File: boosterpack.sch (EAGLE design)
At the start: 38 parts, among them J1 POWERPOLE_DOUBLE, J2 PHOENIXSCREWTERMINAL_2, J3 PHOENIXSCREWTERMINAL_2

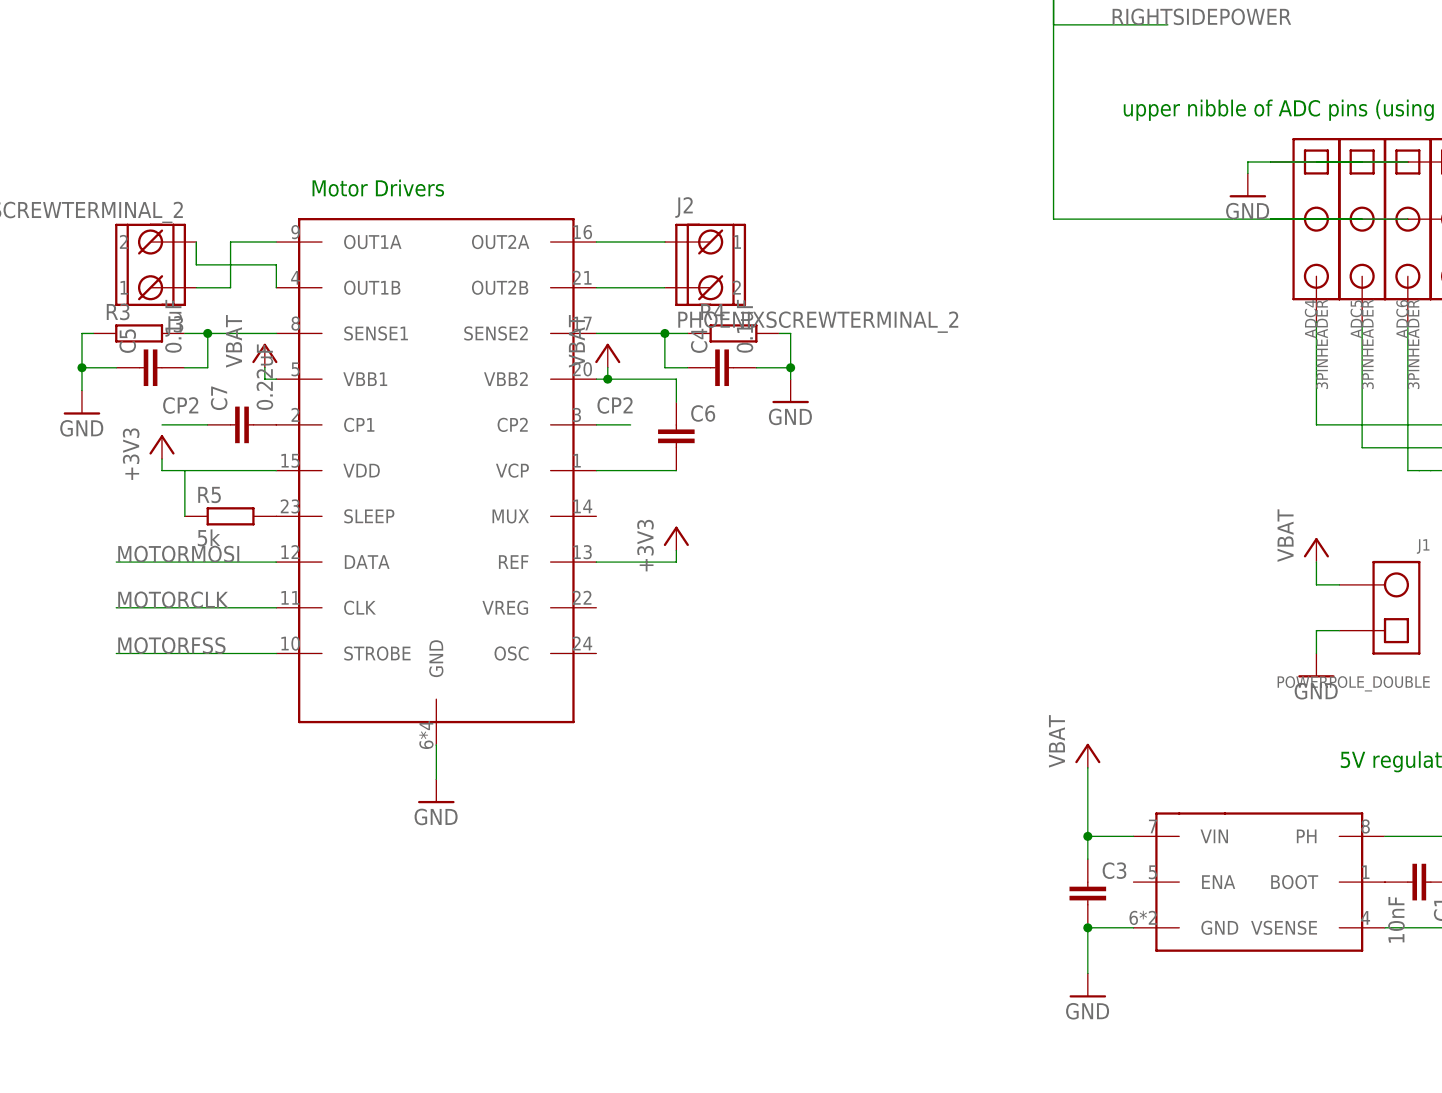
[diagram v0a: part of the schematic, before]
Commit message: shrank the board; added decopling cap for power
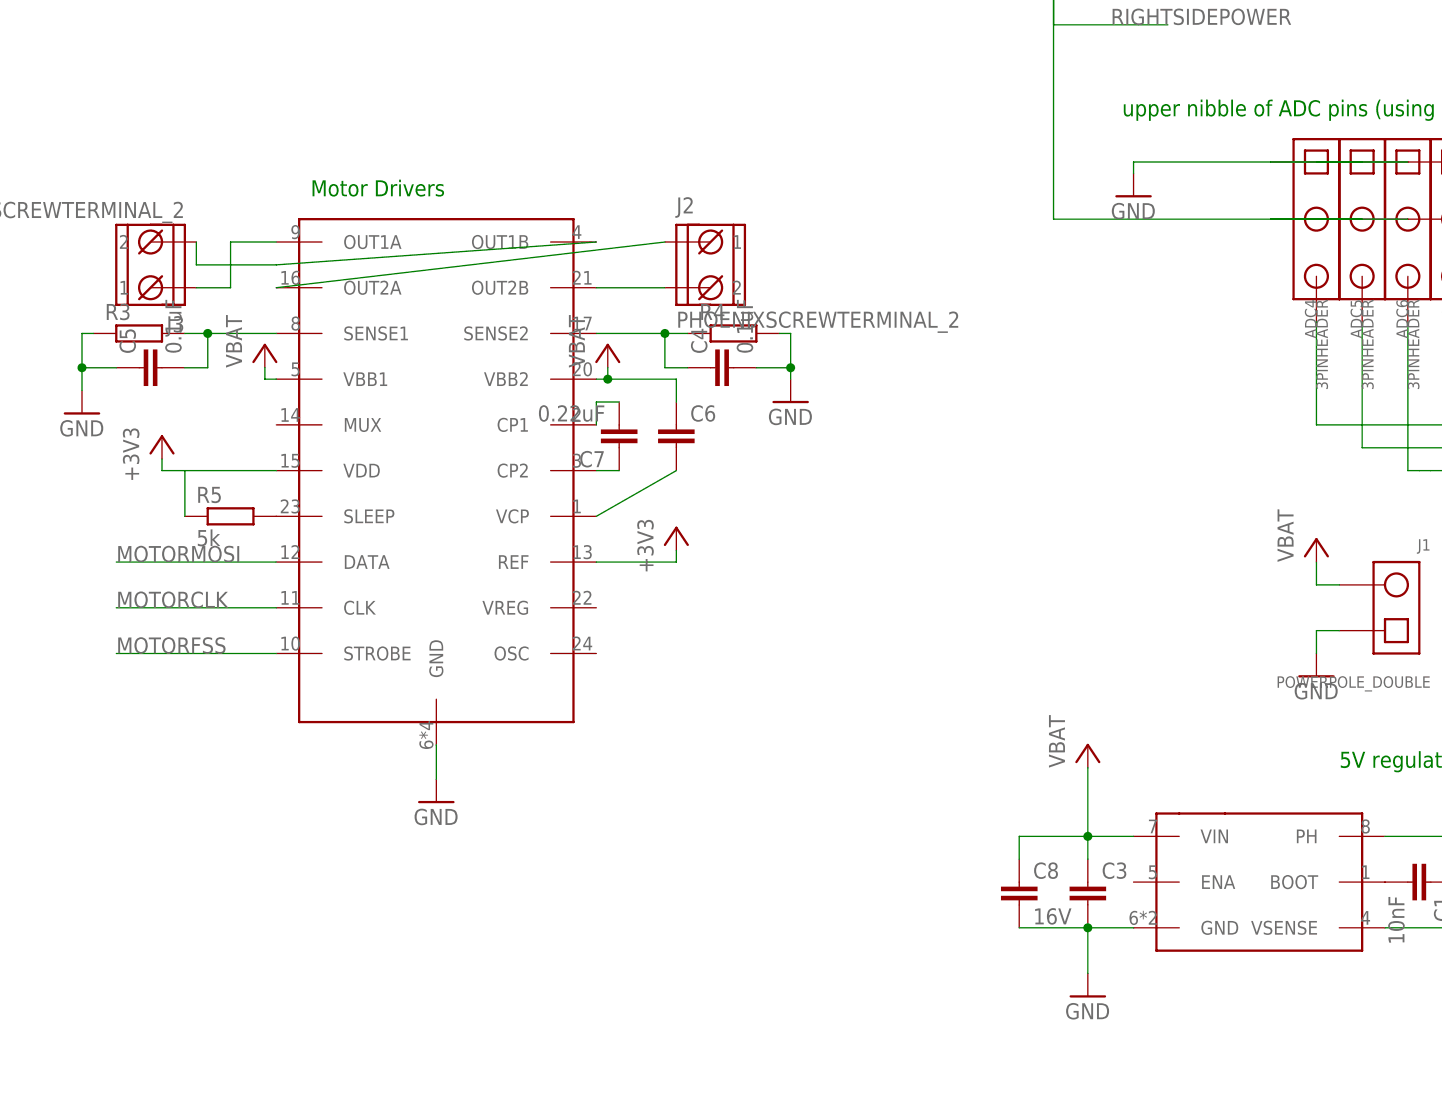
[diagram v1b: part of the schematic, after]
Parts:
- added C8: 16V, resistor:C-EU050-075X075
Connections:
- net CP2 renamed N$23
- net GND: now also C8.2
- net VCC: now also C8.1
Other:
- moved on the sheet: C7
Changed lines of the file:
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@@
 <grid distance="0.05" unitdist="inch" unit="inch" style="lines" multiple="1" display="no" altdistance="0.01" altunitdist="inch" altunit="inch"/>
 <layers>
-<layer number="1" name="Top" color="4" fill="1" visible="yes" active="no"/>
-<layer number="16" name="Bottom" color="1" fill="1" visible="yes" active="no"/>
-<layer number="17" name="Pads" color="2" fill="1" visible="yes" active="no"/>
-<layer number="18" name="Vias" color="2" fill="1" visible="yes" active="no"/>
-<layer number="19" name="Unrouted" color="6" fill="1" visible="yes" active="no"/>
-<layer number="20" name="Dimension" color="15" fill="1" visible="yes" active="no"/>
-<layer number="21" name="tPlace" color="7" fill="1" visible="yes" active="no"/>
-<layer number="22" name="bPlace" color="7" fill="1" visible="yes" active="no"/>
-<layer number="23" name="tOrigins" color="15" fill="1" visible="yes" active="no"/>
-<layer number="24" name="bOrigins" color="15" fill="1" visible="yes" active="no"/>
-<layer number="25" name="tNames" color="7" fill="1" visible="yes" active="no"/>
-<layer number="26" name="bNames" color="7" fill="1" visible="yes" active="no"/>
-<layer number="27" name="tValues" color="7" fill="1" visible="yes" active="no"/>
-<layer number="28" name="bValues" color="7" fill="1" visible="yes" active="no"/>
+<layer number="1" name="Top" color="4" fill="1" visible="no" active="no"/>
+<layer number="16" name="Bottom" color="1" fill="1" visible="no" active="no"/>
+<layer number="17" name="Pads" color="2" fill="1" visible="no" active="no"/>
+<layer number="18" name="Vias" color="2" fill="1" visible="no" active="no"/>
+<layer number="19" name="Unrouted" color="6" fill="1" visible="no" active="no"/>
+<layer number="20" name="Dimension" color="15" fill="1" visible="no" active="no"/>
+<layer number="21" name="tPlace" color="7" fill="1" visible="no" active="no"/>
+<layer number="22" name="bPlace" color="7" fill="1" visible="no" active="no"/>
+<layer number="23" name="tOrigins" color="15" fill="1" visible="no" active="no"/>
+<layer number="24" name="bOrigins" color="15" fill="1" visible="no" active="no"/>
+<layer number="25" name="tNames" color="7" fill="1" visible="no" active="no"/>
+<layer number="26" name="bNames" color="7" fill="1" visible="no" active="no"/>
+<layer number="27" name="tValues" color="7" fill="1" visible="no" active="no"/>
+<layer number="28" name="bValues" color="7" fill="1" visible="no" active="no"/>
 <layer number="29" name="tStop" color="7" fill="3" visible="no" active="no"/>
 <layer number="30" name="bStop" color="7" fill="6" visible="no" active="no"/>
@@
 <layer number="35" name="tGlue" color="7" fill="4" visible="no" active="no"/>
 <layer number="36" name="bGlue" color="7" fill="5" visible="no" active="no"/>
-<layer number="37" name="tTest" color="7" fill="1" visible="yes" active="no"/>
-<layer number="38" name="bTest" color="7" fill="1" visible="yes" active="no"/>
+<layer number="37" name="tTest" color="7" fill="1" visible="no" active="no"/>
+<layer number="38" name="bTest" color="7" fill="1" visible="no" active="no"/>
 <layer number="39" name="tKeepout" color="4" fill="11" visible="no" active="no"/>
 <layer number="40" name="bKeepout" color="1" fill="11" visible="no" active="no"/>
@@
 <layer number="44" name="Drills" color="7" fill="1" visible="no" active="no"/>
 <layer number="45" name="Holes" color="7" fill="1" visible="no" active="no"/>
-<layer number="46" name="Milling" color="3" fill="1" visible="yes" active="no"/>
-<layer number="47" name="Measures" color="7" fill="1" visible="yes" active="no"/>
-<layer number="48" name="Document" color="7" fill="1" visible="yes" active="no"/>
-<layer number="49" name="Reference" color="7" fill="1" visible="yes" active="no"/>
-<layer number="50" name="dxf" color="7" fill="1" visible="yes" active="no"/>
-<layer number="51" name="tDocu" color="7" fill="1" visible="yes" active="no"/>
-<layer number="52" name="bDocu" color="7" fill="1" visible="yes" active="no"/>
-<layer number="53" name="tGND_GNDA" color="7" fill="9" visible="yes" active="no"/>
-<layer number="54" name="bGND_GNDA" color="1" fill="9" visible="yes" active="no"/>
-<layer number="56" name="wert" color="7" fill="1" visible="yes" active="no"/>
-<layer number="59" name="tCarbon" color="7" fill="1" visible="yes" active="no"/>
-<layer number="60" name="bCarbon" color="7" fill="1" visible="yes" active="no"/>
+<layer number="46" name="Milling" color="3" fill="1" visible="no" active="no"/>
+<layer number="47" name="Measures" color="7" fill="1" visible="no" active="no"/>
+<layer number="48" name="Document" color="7" fill="1" visible="no" active="no"/>
+<layer number="49" name="Reference" color="7" fill="1" visible="no" active="no"/>
+<layer number="50" name="dxf" color="7" fill="1" visible="no" active="no"/>
+<layer number="51" name="tDocu" color="7" fill="1" visible="no" active="no"/>
+<layer number="52" name="bDocu" color="7" fill="1" visible="no" active="no"/>
+<layer number="53" name="tGND_GNDA" color="7" fill="9" visible="no" active="no"/>
+<layer number="54" name="bGND_GNDA" color="1" fill="9" visible="no" active="no"/>
+<layer number="56" name="wert" color="7" fill="1" visible="no" active="no"/>
+<layer number="59" name="tCarbon" color="7" fill="1" visible="no" active="no"/>
+<layer number="60" name="bCarbon" color="7" fill="1" visible="no" active="no"/>
 <layer number="91" name="Nets" color="2" fill="1" visible="yes" active="yes"/>
 <layer number="92" name="Busses" color="1" fill="1" visible="yes" active="yes"/>
@@
 <part name="+3V6" library="supply1" deviceset="+3V3" device=""/>
 <part name="+3V7" library="supply1" deviceset="+3V3" device=""/>
+<part name="C8" library="resistor" deviceset="C-EU" device="050-075X075" value="16V"/>
 </parts>
 <sheets>
@@
 <instance part="+3V3" gate="G$1" x="53.34" y="33.02"/>
 <instance part="GND7" gate="1" x="134.62" y="86.36"/>
-<instance part="GND8" gate="1" x="-2.54" y="73.66"/>
+<instance part="GND8" gate="1" x="-15.24" y="73.66"/>
 <instance part="D1" gate="G$1" x="25.4" y="-3.81" rot="R90"/>
 <instance part="U$3" gate="G$1" x="-92.71" y="17.78"/>
@@
 <instance part="C6" gate="G$1" x="-66.04" y="48.26"/>
 <instance part="R5" gate="G$1" x="-115.57" y="38.1"/>
-<instance part="C7" gate="G$1" x="-115.57" y="48.26" rot="R90"/>
+<instance part="C7" gate="G$1" x="-72.39" y="45.72" rot="R180"/>
 <instance part="+3V6" gate="G$1" x="-123.19" y="46.99"/>
 <instance part="+3V7" gate="G$1" x="-66.04" y="36.83"/>
+<instance part="C8" gate="G$1" x="-27.94" y="-2.54"/>
 </instances>
 <busses>
@@
 <wire x1="-20.32" y1="-7.62" x2="-15.24" y2="-7.62" width="0.1524" layer="91"/>
 <junction x="-20.32" y="-7.62"/>
+<pinref part="C8" gate="G$1" pin="2"/>
+<wire x1="-20.32" y1="-7.62" x2="-27.94" y2="-7.62" width="0.1524" layer="91"/>
 </segment>
 <segment>
@@
 <pinref part="ADC4" gate="G$1" pin="1"/>
 <pinref part="GND8" gate="1" pin="GND"/>
-<wire x1="0" y1="77.47" x2="-2.54" y2="77.47" width="0.1524" layer="91"/>
+<wire x1="0" y1="77.47" x2="-15.24" y2="77.47" width="0.1524" layer="91"/>
 <pinref part="ADC5" gate="G$1" pin="1"/>
 <pinref part="ADC6" gate="G$1" pin="1"/>
@@
 <wire x1="15.24" y1="77.47" x2="5.08" y2="77.47" width="0.1524" layer="91"/>
 <wire x1="5.08" y1="77.47" x2="0" y2="77.47" width="0.1524" layer="91"/>
-<wire x1="-2.54" y1="77.47" x2="-2.54" y2="76.2" width="0.1524" layer="91"/>
+<wire x1="-15.24" y1="77.47" x2="-15.24" y2="76.2" width="0.1524" layer="91"/>
 </segment>
 <segment>
@@
 <wire x1="-20.32" y1="10.16" x2="-20.32" y2="2.54" width="0.1524" layer="91"/>
 <junction x="-20.32" y="2.54"/>
+<pinref part="C8" gate="G$1" pin="1"/>
+<wire x1="-20.32" y1="2.54" x2="-27.94" y2="2.54" width="0.1524" layer="91"/>
+<wire x1="-27.94" y1="2.54" x2="-27.94" y2="0" width="0.1524" layer="91"/>
 </segment>
 <segment>
@@
 <pinref part="J2" gate="G$1" pin="1"/>
 <pinref part="U$3" gate="G$1" pin="OUT2A"/>
-<wire x1="-67.31" y1="68.58" x2="-74.93" y2="68.58" width="0.1524" layer="91"/>
+<wire x1="-67.31" y1="68.58" x2="-110.49" y2="63.5" width="0.1524" layer="91"/>
 </segment>
 </net>
@@
 <pinref part="U$3" gate="G$1" pin="VCP"/>
 <pinref part="C6" gate="G$1" pin="2"/>
-<wire x1="-74.93" y1="43.18" x2="-66.04" y2="43.18" width="0.1524" layer="91"/>
+<wire x1="-74.93" y1="38.1" x2="-66.04" y2="43.18" width="0.1524" layer="91"/>
 </segment>
 </net>
@@
 <pinref part="U$3" gate="G$1" pin="SLEEP"/>
 <pinref part="R5" gate="G$1" pin="2"/>
-</segment>
-</net>
-<net name="CP2" class="0">
-<segment>
-<pinref part="U$3" gate="G$1" pin="CP2"/>
-<wire x1="-74.93" y1="48.26" x2="-71.12" y2="48.26" width="0.1524" layer="91"/>
-<label x="-74.93" y="49.53" size="1.778" layer="95"/>
-</segment>
-<segment>
-<pinref part="C7" gate="G$1" pin="1"/>
-<wire x1="-118.11" y1="48.26" x2="-123.19" y2="48.26" width="0.1524" layer="91"/>
-<label x="-123.19" y="49.53" size="1.778" layer="95"/>
-</segment>
-</net>
-<net name="N$23" class="0">
-<segment>
-<pinref part="U$3" gate="G$1" pin="CP1"/>
-<pinref part="C7" gate="G$1" pin="2"/>
 </segment>
 </net>
@@
 <segment>
 <pinref part="U$3" gate="G$1" pin="OUT1B"/>
-<wire x1="-110.49" y1="63.5" x2="-110.49" y2="66.04" width="0.1524" layer="91"/>
+<wire x1="-74.93" y1="68.58" x2="-110.49" y2="66.04" width="0.1524" layer="91"/>
 <pinref part="J3" gate="G$1" pin="2"/>
 <wire x1="-110.49" y1="66.04" x2="-119.38" y2="66.04" width="0.1524" layer="91"/>
@@
 </segment>
 </net>
+<net name="N$23" class="0">
+<segment>
+<pinref part="U$3" gate="G$1" pin="CP2"/>
+<pinref part="C7" gate="G$1" pin="1"/>
+<wire x1="-74.93" y1="43.18" x2="-72.39" y2="43.18" width="0.1524" layer="91"/>
+</segment>
+</net>
+<net name="N$28" class="0">
+<segment>
+<pinref part="C7" gate="G$1" pin="2"/>
+<pinref part="U$3" gate="G$1" pin="CP1"/>
+<wire x1="-72.39" y1="50.8" x2="-74.93" y2="50.8" width="0.1524" layer="91"/>
+<wire x1="-74.93" y1="50.8" x2="-74.93" y2="48.26" width="0.1524" layer="91"/>
+</segment>
+</net>

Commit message: increased the spacing between the leads of all resistors and some caps
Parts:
- C2: device resistor:CPOL-EUB45181A -> rcl:CPOL-EUB45181B
- D1: device diode:SCHOTTKY-DIODEDO35-7 -> diode:SCHOTTKY-DIODEDO201T15
- R1, R2, R3, R4, R5: device resistor:R-EU_0204/5 -> rcl:R-EU_0204/7
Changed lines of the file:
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@@
 <setting verticaltext="up"/>
 </settings>
-<grid distance="0.05" unitdist="inch" unit="inch" style="lines" multiple="1" display="no" altdistance="0.01" altunitdist="inch" altunit="inch"/>
+<grid distance="0.1" unitdist="inch" unit="inch" style="lines" multiple="1" display="no" altdistance="0.01" altunitdist="inch" altunit="inch"/>
 <layers>
 <layer number="1" name="Top" color="4" fill="1" visible="no" active="no"/>
@@
 <part name="C1" library="resistor" deviceset="C-EU" device="025-024X044" value="10nF"/>
 <part name="L1" library="RASEagleLib" deviceset="SDR1006" device="" value="10uH"/>
-<part name="R1" library="resistor" deviceset="R-EU_" device="0204/5" value="10k"/>
-<part name="R2" library="resistor" deviceset="R-EU_" device="0204/5" value="3.24k"/>
-<part name="C2" library="resistor" deviceset="CPOL-EU" device="B45181A" value="330uF"/>
+<part name="R1" library="rcl" deviceset="R-EU_" device="0204/7" value="10k"/>
+<part name="R2" library="rcl" deviceset="R-EU_" device="0204/7" value="3.24k"/>
+<part name="C2" library="rcl" deviceset="CPOL-EU" device="B45181B" value="330uF"/>
 <part name="GND1" library="supply1" deviceset="GND" device=""/>
 <part name="GND2" library="supply1" deviceset="GND" device=""/>
@@
 <part name="GND7" library="supply1" deviceset="GND" device=""/>
 <part name="GND8" library="supply1" deviceset="GND" device=""/>
-<part name="D1" library="diode" deviceset="SCHOTTKY-DIODE" device="DO35-7"/>
+<part name="D1" library="diode" deviceset="SCHOTTKY-DIODE" device="DO201T15"/>
 <part name="U$3" library="RASEagleLib" deviceset="A3992" device="A"/>
 <part name="GND9" library="supply1" deviceset="GND" device=""/>
@@
 <part name="P+7" library="supply1" deviceset="VCC" device="" value="VBAT"/>
 <part name="P+8" library="supply1" deviceset="VCC" device="" value="VBAT"/>
-<part name="R3" library="resistor" deviceset="R-EU_" device="0204/5"/>
-<part name="R4" library="resistor" deviceset="R-EU_" device="0204/5"/>
+<part name="R3" library="rcl" deviceset="R-EU_" device="0204/7"/>
+<part name="R4" library="rcl" deviceset="R-EU_" device="0204/7"/>
 <part name="C4" library="resistor" deviceset="C-EU" device="025-025X050" value="0.1uF"/>
 <part name="C5" library="resistor" deviceset="C-EU" device="025-025X050" value="0.1uF"/>
 <part name="C6" library="resistor" deviceset="C-EU" device="025-025X050"/>
-<part name="R5" library="resistor" deviceset="R-EU_" device="0204/5" value="5k"/>
+<part name="R5" library="rcl" deviceset="R-EU_" device="0204/7" value="5k"/>
 <part name="C7" library="resistor" deviceset="C-EU" device="025-024X044" value="0.22uF"/>
 <part name="+3V6" library="supply1" deviceset="+3V3" device=""/>
